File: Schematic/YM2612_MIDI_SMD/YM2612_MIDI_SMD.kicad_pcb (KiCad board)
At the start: 2 copper layers, 100 x 100 mm, 112 parts, among them J1 DIN-5_180, J3 USB_B, J5 ICSP, J6 Audio-Jack-3, J7 Micro_SD_Card, SW1 Rotary_Encoder_Switch, SW10 SW_Push_Dual, SW2 SW_Push_Dual, SW3 SW_Push_Dual, SW4 SW_Push_Dual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

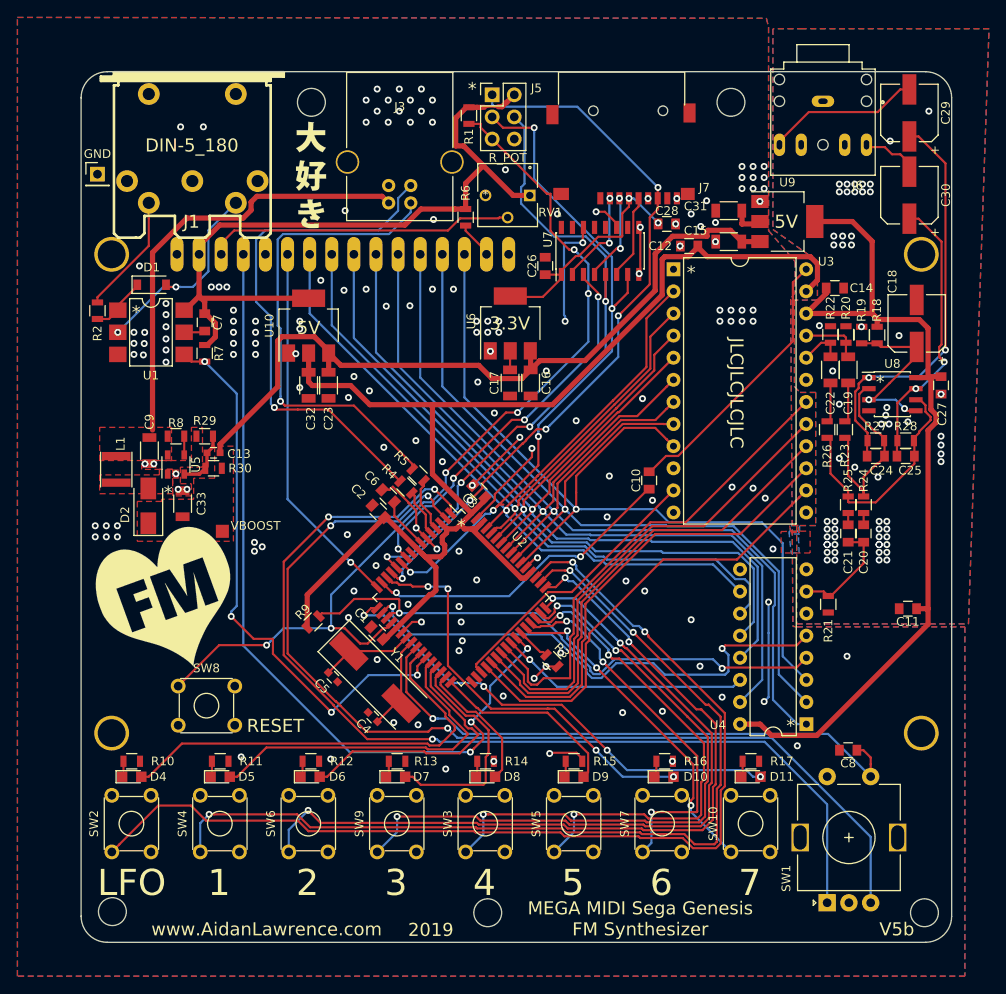
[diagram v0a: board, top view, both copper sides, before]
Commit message: PSG Noise support on MIDI CH. 5
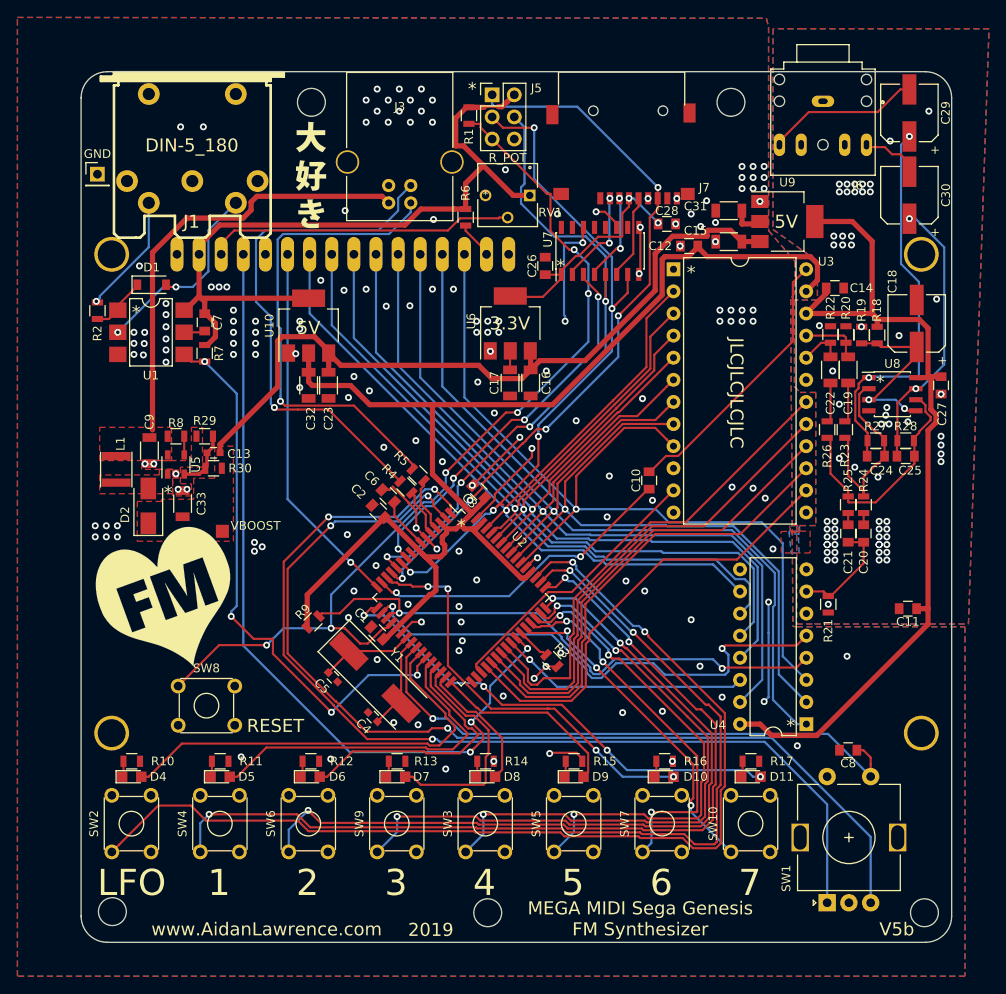
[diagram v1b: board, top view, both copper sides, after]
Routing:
- net Net-(C24-Pad1): track 47.5 -> 45.2 mm
- net Net-(J1-Pad4): track 13.9 -> 13.8 mm, vias 0 -> 1
- net GND: vias 233 -> 235
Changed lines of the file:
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@@
   (general
     (thickness 1.6)
-    (drawings 39)
-    (tracks 1604)
+    (drawings 40)
+    (tracks 1602)
     (zones 0)
     (modules 112)
@@
       (net 125 VBOOST))
   )
+  (gr_text * (at 228.092 67.31) (layer F.SilkS)
+    (effects (font (size 1.5 1.5) (thickness 0.3)))
+  )
   (gr_text * (at 264.795 80.645) (layer F.SilkS)
     (effects (font (size 1.5 1.5) (thickness 0.3)))
@@
     (effects (font (size 3 3) (thickness 0.3)))
   )
+  (via (at 174.752 71.374) (size 0.8) (drill 0.4) (layers F.Cu B.Cu) (net 98))
   (via (at 181.356 90.043) (size 0.8) (drill 0.4) (layers F.Cu B.Cu) (net 1))
   (via (at 180.34 90.043) (size 0.8) (drill 0.4) (layers F.Cu B.Cu) (net 1))
@@
   (via (at 174.625 98.425) (size 0.8) (drill 0.4) (layers F.Cu B.Cu) (net 1))
   (via (at 179.705 67.31) (size 0.8) (drill 0.4) (layers F.Cu B.Cu) (net 1))
+  (via (at 258.826 106.172) (size 0.8) (drill 0.4) (layers F.Cu B.Cu) (net 1))
+  (via (at 271.272 71.12) (size 0.8) (drill 0.4) (layers F.Cu B.Cu) (net 1))
   (segment (start 219.202 49.022) (end 218.526001 49.022) (width 0.25) (layer F.Cu) (net 2))
   (segment (start 220.782001 49.015399) (end 220.788602 49.022) (width 0.25) (layer F.Cu) (net 2))
@@
   (segment (start 266.766 87.376) (end 266.766 83.058) (width 0.25) (layer F.Cu) (net 7))
   (via (at 268.892 81.407) (size 0.8) (drill 0.4) (layers F.Cu B.Cu) (net 7))
-  (segment (start 271.837989 64.522189) (end 271.837989 76.339007) (width 0.25) (layer F.Cu) (net 7))
-  (segment (start 272.142704 78.631296) (end 272.142704 78.3324) (width 0.25) (layer B.Cu) (net 7))
-  (segment (start 271.562998 77.752694) (end 271.742705 77.932401) (width 0.25) (layer F.Cu) (net 7))
   (segment (start 269.367 81.407) (end 272.142704 78.631296) (width 0.25) (layer B.Cu) (net 7))
   (segment (start 268.892 81.407) (end 269.367 81.407) (width 0.25) (layer B.Cu) (net 7))
-  (segment (start 271.562998 76.613998) (end 271.562998 77.752694) (width 0.25) (layer F.Cu) (net 7))
-  (segment (start 271.742705 77.932401) (end 272.142704 78.3324) (width 0.25) (layer F.Cu) (net 7))
-  (segment (start 271.837989 76.339007) (end 271.562998 76.613998) (width 0.25) (layer F.Cu) (net 7))
-  (segment (start 269.1978 61.882) (end 271.837989 64.522189) (width 0.25) (layer F.Cu) (net 7))
-  (segment (start 268.1478 61.882) (end 269.1978 61.882) (width 0.25) (layer F.Cu) (net 7))
-  (via (at 272.142704 78.3324) (size 0.8) (drill 0.4) (layers F.Cu B.Cu) (net 7))
+  (via (at 268.1478 61.882) (size 0.8) (drill 0.4) (layers F.Cu B.Cu) (net 7))
+  (segment (start 268.863002 61.882) (end 268.1478 61.882) (width 0.25) (layer B.Cu) (net 7))
+  (segment (start 272.142704 65.161702) (end 268.863002 61.882) (width 0.25) (layer B.Cu) (net 7))
+  (segment (start 272.142704 78.631296) (end 272.142704 65.161702) (width 0.25) (layer B.Cu) (net 7))
   (segment (start 259.08 104.968) (end 258.826 105.222) (width 0.25) (layer F.Cu) (net 8))
   (segment (start 258.3028 104.6988) (end 258.826 105.222) (width 0.25) (layer F.Cu) (net 8))
@@
   (segment (start 248.986 125.834) (end 248.836 125.984) (width 0.25) (layer F.Cu) (net 96))
   (segment (start 248.986 124.206) (end 248.986 125.834) (width 0.25) (layer F.Cu) (net 96))
-  (segment (start 180.7756 61.826966) (end 180.7756 60.0592) (width 0.25) (layer F.Cu) (net 98))
-  (segment (start 180.7756 65.0044) (end 180.7756 61.826966) (width 0.25) (layer F.Cu) (net 98))
-  (segment (start 174.879 70.901) (end 180.7756 65.0044) (width 0.25) (layer F.Cu) (net 98))
-  (segment (start 174.879 71.501) (end 174.879 70.901) (width 0.25) (layer F.Cu) (net 98))
+  (segment (start 175.151999 70.974001) (end 174.752 71.374) (width 0.25) (layer B.Cu) (net 98))
+  (segment (start 175.151999 70.773003) (end 175.151999 70.974001) (width 0.25) (layer B.Cu) (net 98))
+  (segment (start 180.7756 65.149402) (end 175.151999 70.773003) (width 0.25) (layer B.Cu) (net 98))
+  (segment (start 180.7756 60.0592) (end 180.7756 65.149402) (width 0.25) (layer B.Cu) (net 98))
   (segment (start 234.5182 67.8328) (end 234.5182 68.2828) (width 0.25) (layer F.Cu) (net 102))
   (segment (start 236.433199 65.917801) (end 234.5182 67.8328) (width 0.25) (layer F.Cu) (net 102))
@@
   (segment (start 263.287 87.426) (end 263.337 87.376) (width 0.25) (layer F.Cu) (net 110))
   (segment (start 263.287 89.154) (end 263.287 87.426) (width 0.25) (layer F.Cu) (net 110))
-  (segment (start 272.288 55.5234) (end 272.288 76.962) (width 0.25) (layer F.Cu) (net 110))
-  (segment (start 268.1478 52.4332) (end 269.1978 52.4332) (width 0.25) (layer F.Cu) (net 110))
-  (segment (start 269.1978 52.4332) (end 272.288 55.5234) (width 0.25) (layer F.Cu) (net 110))
-  (via (at 272.288 76.962) (size 0.8) (drill 0.4) (layers F.Cu B.Cu) (net 110))
   (via (at 263.492 80.137) (size 0.8) (drill 0.4) (layers F.Cu B.Cu) (net 110))
   (segment (start 263.619 80.01) (end 263.492 80.137) (width 0.25) (layer B.Cu) (net 110))
   (segment (start 269.24 80.01) (end 263.619 80.01) (width 0.25) (layer B.Cu) (net 110))
-  (segment (start 272.288 76.962) (end 269.24 80.01) (width 0.25) (layer B.Cu) (net 110))
   (segment (start 261.931989 81.728601) (end 262.312991 81.347599) (width 0.25) (layer F.Cu) (net 110))
   (segment (start 262.312991 81.347599) (end 262.312991 80.841009) (width 0.25) (layer F.Cu) (net 110))
@@
   (segment (start 263.337 86.476) (end 261.931989 85.070989) (width 0.25) (layer F.Cu) (net 110))
   (segment (start 263.017 80.137) (end 263.492 80.137) (width 0.25) (layer F.Cu) (net 110))
+  (via (at 268.1478 52.4332) (size 0.8) (drill 0.4) (layers F.Cu B.Cu) (net 110))
+  (segment (start 267.186999 53.394001) (end 268.1478 52.4332) (width 0.25) (layer B.Cu) (net 110))
+  (segment (start 267.186999 67.088001) (end 267.186999 53.394001) (width 0.25) (layer B.Cu) (net 110))
+  (segment (start 269.24 69.141002) (end 267.186999 67.088001) (width 0.25) (layer B.Cu) (net 110))
+  (segment (start 269.24 80.01) (end 269.24 69.141002) (width 0.25) (layer B.Cu) (net 110))
   (segment (start 261.112 80.748) (end 261.112 85.156) (width 0.25) (layer F.Cu) (net 111))
   (segment (start 262.89 97.044) (end 262.89 95.692) (width 0.25) (layer F.Cu) (net 112))
